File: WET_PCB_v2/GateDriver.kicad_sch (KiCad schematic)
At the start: 12 parts, among them U5 IR2110

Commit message: most routing done. to do: 12v routing, test points, deco, checking clearance
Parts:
- D13, D14: footprint Diode_THT:D_A-405_P2.54mm_Vertical_CathodeUp -> Diode_THT:D_A-405_P7.62mm_Horizontal
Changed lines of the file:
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@@
 			)
 		)
-		(property "Footprint" "Diode_THT:D_A-405_P2.54mm_Vertical_CathodeUp"
+		(property "Footprint" "Diode_THT:D_A-405_P7.62mm_Horizontal"
 			(at 135.89 92.075 0)
 			(hide yes)
@@
 			)
 		)
-		(property "Footprint" "Diode_THT:D_A-405_P2.54mm_Vertical_CathodeUp"
+		(property "Footprint" "Diode_THT:D_A-405_P7.62mm_Horizontal"
 			(at 135.89 57.785 0)
 			(hide yes)

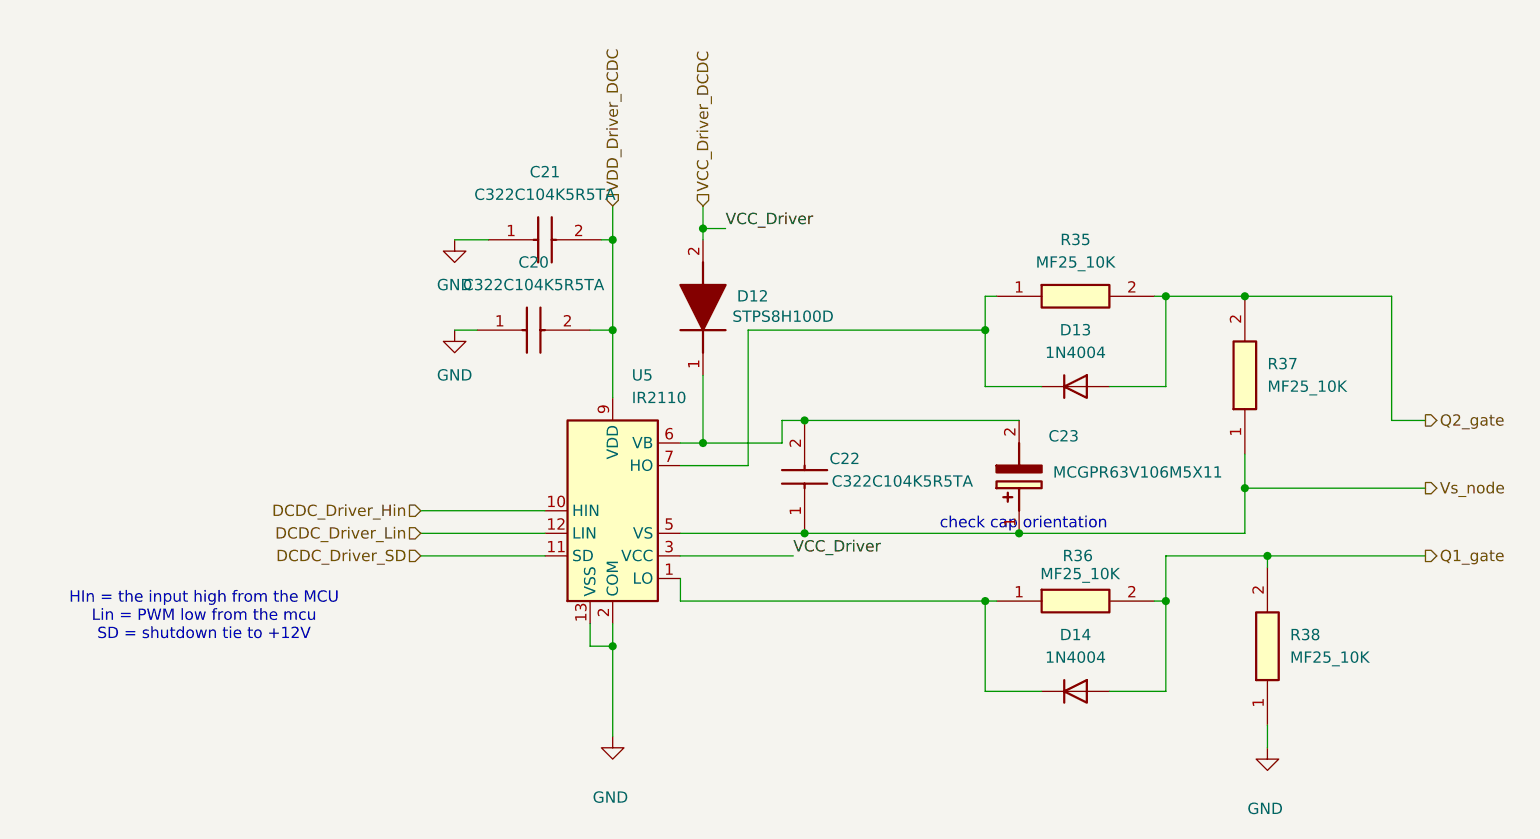
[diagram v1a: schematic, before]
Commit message: some caps were missing and wrong way around AAAAAAAAAAAAAAAAAAAAAAAAAAAAAAAAAAA
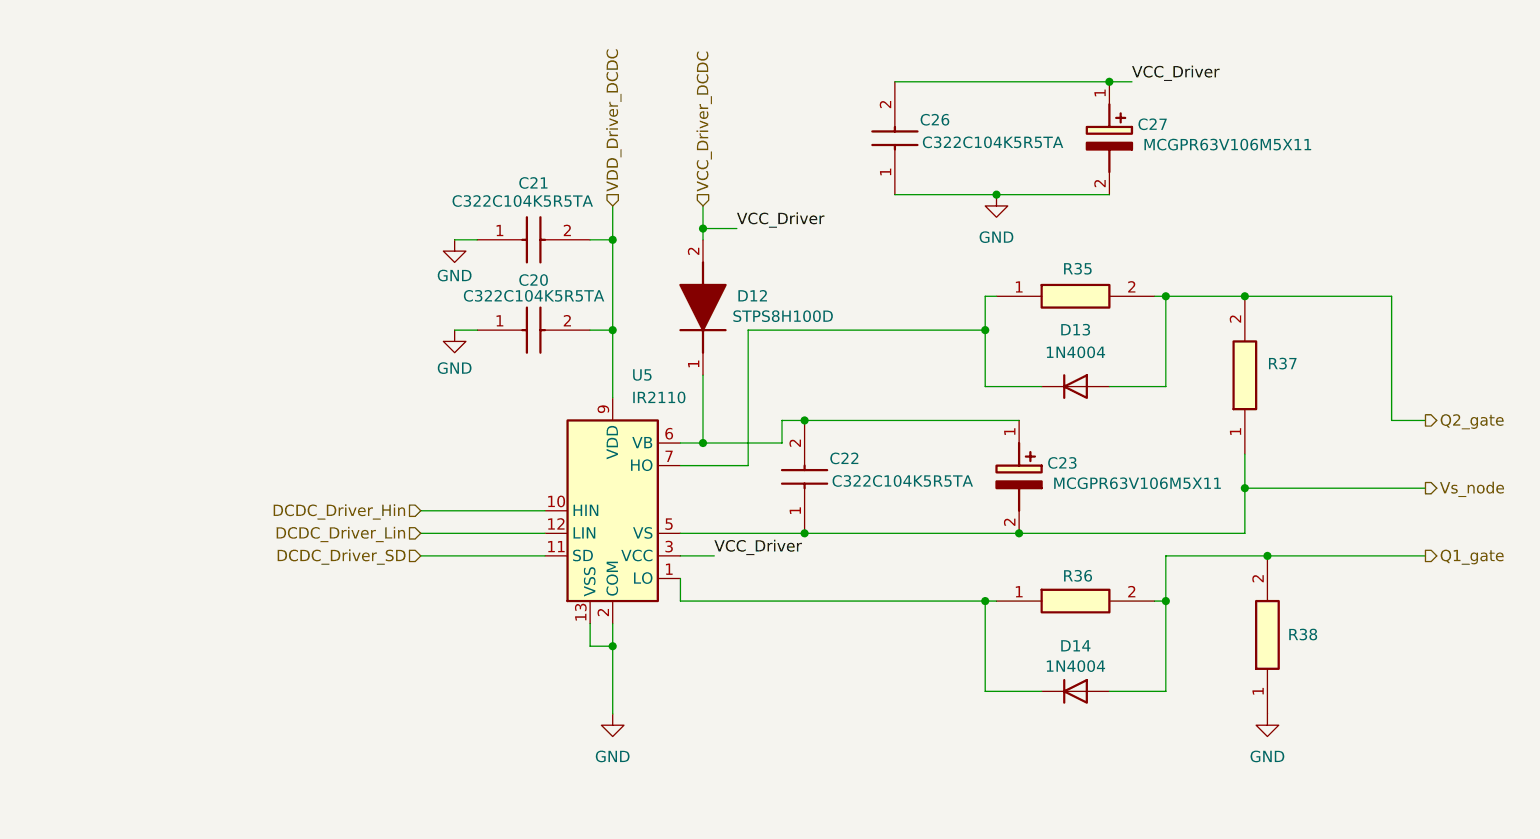
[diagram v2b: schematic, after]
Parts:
- added C26: C322C104K5R5TA, Capacitor_THT:C_Disc_D4.3mm_W1.9mm_P5.00mm, symbol C322C104K5R5TA:C322C104K5R5TA
- added C27: MCGPR63V106M5X11, Capacitor_THT:C_Radial_D5.0mm_H11.0mm_P2.00mm, symbol MCGPR63V106M5X11:MCGPR63V106M5X11
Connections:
- net GND: now also C26.1, C27.2 (-)
- net VCC_Driver_DCDC: now also C26.2, C27.1 (+)
- net Vs_node: now also C23.2 (-); no longer C23.1 (+)
- net at C22.2, D12.1 (K), U5.6 (VB): now also C23.1 (+); no longer C23.2 (-)
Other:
- note removed: "HIn = the input high from the MCU Lin = PWM low from the mcu SD = shutdown tie to +12V"
- note removed: "check cap orientation"
- moved on the sheet: C21, R38

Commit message: added values and notes for assembly
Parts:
- R35, R36: value MF25_10K -> 10R
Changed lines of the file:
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@@
 			)
 		)
-		(property "Value" "MF25_10K"
+		(property "Value" "10R"
 			(at 136.398 74.422 0)
 			(hide yes)
@@
 			)
 		)
-		(property "Value" "MF25_10K"
+		(property "Value" "10R"
 			(at 135.89 39.37 0)
 			(hide yes)
